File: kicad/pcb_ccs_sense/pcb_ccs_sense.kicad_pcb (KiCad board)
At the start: 2 copper layers, 120 x 80 mm, 6 parts

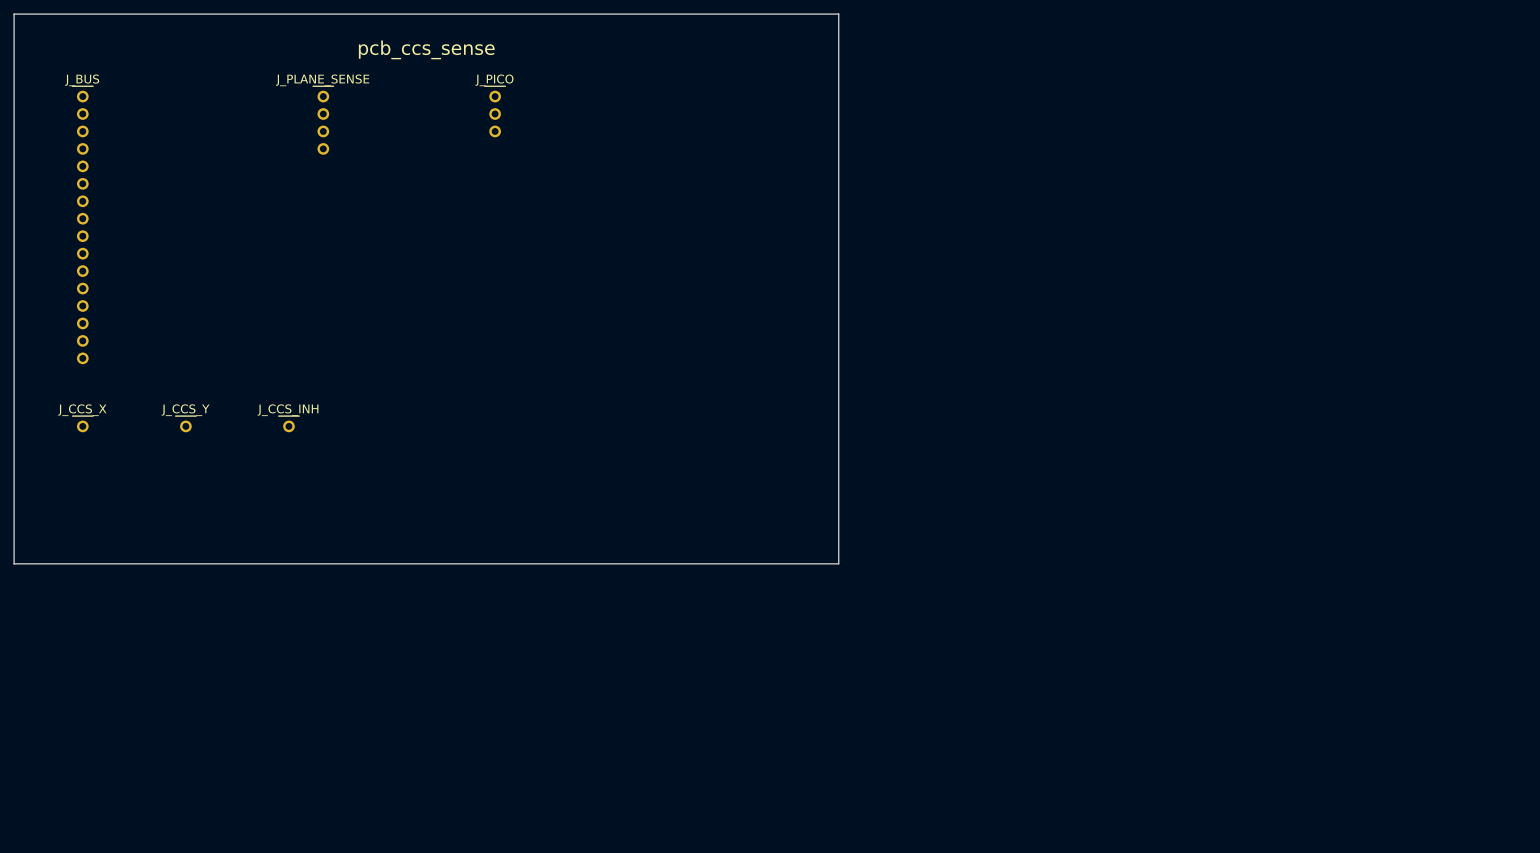
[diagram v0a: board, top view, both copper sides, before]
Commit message: logical seperation into host and multiple decode/drive/steering boards
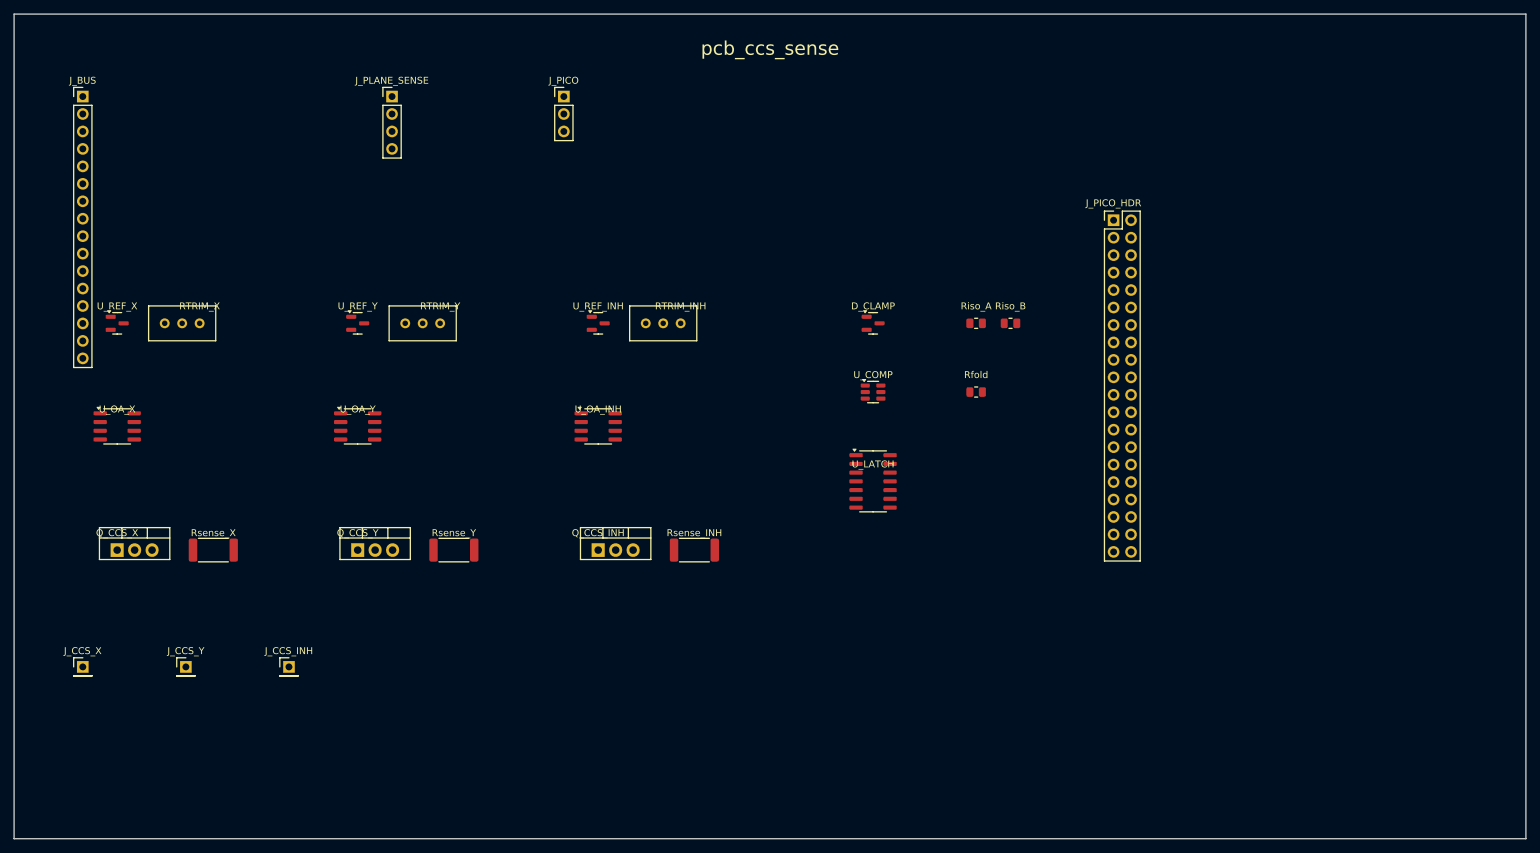
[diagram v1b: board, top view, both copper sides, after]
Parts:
- added D_CLAMP: BAT54S, Package_TO_SOT_SMD:SOT-23, F.Cu at (125.0, 45.0)
- added J_PICO_HDR: Pico_Header, Connector_PinHeader_2.54mm:PinHeader_2x20_P2.54mm_Vertical, F.Cu at (160.0, 30.0)
- added Q_CCS_INH: IRLZ44N, Package_TO_SOT_THT:TO-220-3_Vertical, F.Cu at (85.0, 78.0)
- added Q_CCS_X: IRLZ44N, Package_TO_SOT_THT:TO-220-3_Vertical, F.Cu at (15.0, 78.0)
- added Q_CCS_Y: IRLZ44N, Package_TO_SOT_THT:TO-220-3_Vertical, F.Cu at (50.0, 78.0)
- added RTRIM_INH: 3296W, Potentiometer_THT:Potentiometer_Bourns_3296W_Vertical, F.Cu at (97.0, 45.0)
- added RTRIM_X: 3296W, Potentiometer_THT:Potentiometer_Bourns_3296W_Vertical, F.Cu at (27.0, 45.0)
- added RTRIM_Y: 3296W, Potentiometer_THT:Potentiometer_Bourns_3296W_Vertical, F.Cu at (62.0, 45.0)
- added Rfold: 10k, Resistor_SMD:R_0805_2012Metric, F.Cu at (140.0, 55.0)
- added Riso_A: 1k, Resistor_SMD:R_0805_2012Metric, F.Cu at (140.0, 45.0)
- added Riso_B: 1k, Resistor_SMD:R_0805_2012Metric, F.Cu at (145.0, 45.0)
- added Rsense_INH: 1R0, Resistor_SMD:R_2512_6332Metric, F.Cu at (99.0, 78.0)
- added Rsense_X: 1R0, Resistor_SMD:R_2512_6332Metric, F.Cu at (29.0, 78.0)
- added Rsense_Y: 1R0, Resistor_SMD:R_2512_6332Metric, F.Cu at (64.0, 78.0)
- added U_COMP: TLV3501, Package_TO_SOT_SMD:SOT-23-6, F.Cu at (125.0, 55.0)
- added U_LATCH: 74AHC74, Package_SO:SOIC-14_3.9x8.7mm_P1.27mm, F.Cu at (125.0, 68.0)
- added U_OA_INH: OPA192, Package_SO:SOIC-8_3.9x4.9mm_P1.27mm, F.Cu at (85.0, 60.0)
- added U_OA_X: OPA192, Package_SO:SOIC-8_3.9x4.9mm_P1.27mm, F.Cu at (15.0, 60.0)
- added U_OA_Y: OPA192, Package_SO:SOIC-8_3.9x4.9mm_P1.27mm, F.Cu at (50.0, 60.0)
- added U_REF_INH: TL431, Package_TO_SOT_SMD:SOT-23, F.Cu at (85.0, 45.0)
- added U_REF_X: TL431, Package_TO_SOT_SMD:SOT-23, F.Cu at (15.0, 45.0)
- added U_REF_Y: TL431, Package_TO_SOT_SMD:SOT-23, F.Cu at (50.0, 45.0)
- J_CCS_INH, J_CCS_X, J_CCS_Y: footprint Connector_PinHeader_2.54mm:PinHeader_1x1_P2.54mm_Vertical -> Connector_PinHeader_2.54mm:PinHeader_1x01_P2.54mm_Vertical
- J_PICO: footprint Connector_PinHeader_2.54mm:PinHeader_1x3_P2.54mm_Vertical -> Connector_PinHeader_2.54mm:PinHeader_1x03_P2.54mm_Vertical
- J_PLANE_SENSE: footprint Connector_PinHeader_2.54mm:PinHeader_1x4_P2.54mm_Vertical -> Connector_PinHeader_2.54mm:PinHeader_1x04_P2.54mm_Vertical
- moved J_CCS_INH 35.0 mm to (40.0, 95.0)
- moved J_CCS_X 35.0 mm to (10.0, 95.0)
- moved J_CCS_Y 35.0 mm to (25.0, 95.0)
- moved J_PICO 10.0 mm to (80.0, 12.0)
- moved J_PLANE_SENSE 10.0 mm to (55.0, 12.0)
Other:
- board size 120 x 80 mm -> 220 x 120 mm
